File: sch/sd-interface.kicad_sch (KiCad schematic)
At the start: 33 parts, among them J15 F32Q-1A7H1-11022, J16 MEM2075-00-140-01-A, J17 5V_out, J19 3V3_in, Q1 Q_PMOS_GSD, U10 CD4043BDR, U11 TPS22919DCKR, U8 MAX4996LETG_

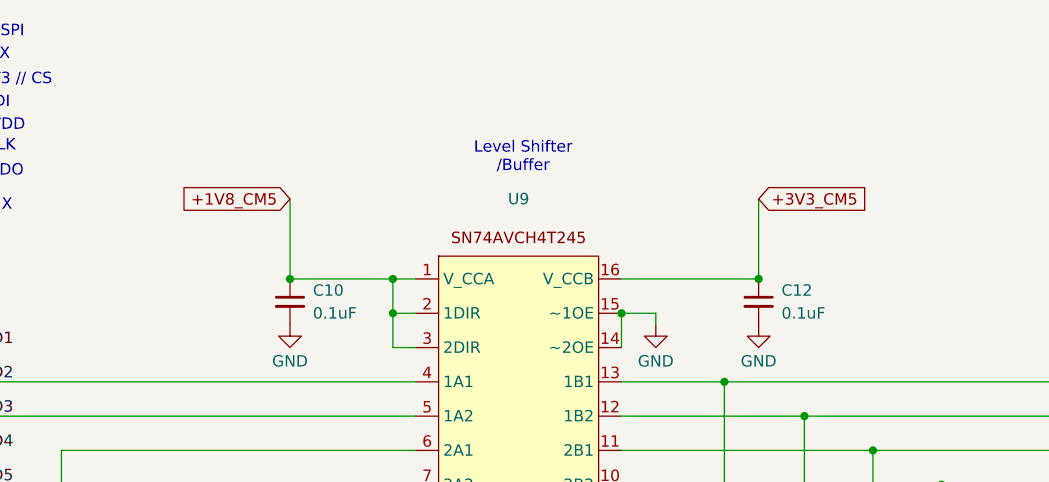
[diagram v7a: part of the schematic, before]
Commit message: fix annotation and clean up schematics
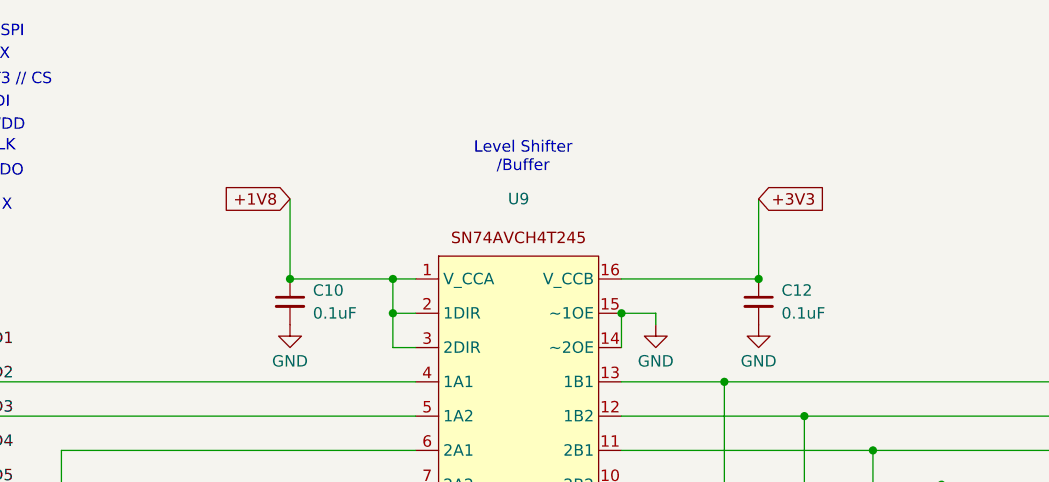
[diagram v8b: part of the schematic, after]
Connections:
- net +1V8_CM5 renamed +1V8
- net +3V3_CM5 renamed +3V3
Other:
- company: (none) -> NTNU, NINA
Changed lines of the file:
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@@
 	(generator_version "9.0")
 	(paper "A3")
+	(title_block
+		(date "2026-02-13")
+		(rev "0")
+		(company "NTNU, NINA")
+		(comment 1 "https://github.com/oveljosland/audiograb-pcb/")
+		(comment 2 "GNU Affero General Public Licence Version 3")
+	)
 	(text "power switch for \noutput device"
 		(exclude_from_sim no)
@@
 		)
 	)
-	(global_label "+3V3_CM5"
+	(global_label "+3V3"
 		(shape input)
 		(at 222.25 34.29 0)
@@
 		)
 		(property "Intersheetrefs" "${INTERSHEET_REFS}"
-			(at 235.2137 34.29 0)
+			(at 230.3152 34.29 0)
 			(effects
 				(font
@@
 		)
 	)
-	(global_label "+1V8_CM5"
+	(global_label "+1V8"
 		(shape input)
 		(at 170.18 34.29 180)
@@
 		)
 		(property "Intersheetrefs" "${INTERSHEET_REFS}"
-			(at 157.2163 34.29 0)
+			(at 162.1148 34.29 0)
 			(effects
 				(font
